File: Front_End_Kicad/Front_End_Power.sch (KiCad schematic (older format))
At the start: 27 parts

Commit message: Added footprints and digikey links to many of the components.  Missing is the primary amplifier
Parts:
- removed C?: C, symbol Device:C
- added C?: 10uF, Capacitor_SMD:C_1206_3216Metric, symbol Device:C
- C202, C203, C205, C206, C207, C208: renamed from C?; footprint (none) -> Capacitor_SMD:C_1206_3216Metric; part_url (none) -> https://www.digikey.com/en/products/detail/taiyo-yuden/EMK3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
- C204: renamed from C?; footprint (none) -> Capacitor_SMD:C_1206_3216Metric; part_url (none) -> https://www.digikey.com/en/products/detail/w%C3%BCrth-elekt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
- U201: renamed from U?; footprint (none) -> Package_TO_SOT_SMD:SOT-23-5
- gave numbers to parts that had none: 18
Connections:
- net at U201.3 (C1-): now also C?.1
- net at U201.5 (C1+): now also C?.2
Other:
- note added: "DC Offset Indication\n\n"
- moved on the sheet: C203, C204, D202, D204, D205, R201, R202, R204, TP201

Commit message: Started work on PCB.  Sections seperated and partially connected.  Planning 4 layer
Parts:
- TP201, TP202, TP203: footprint TestPoint:TestPoint_THTPad_3.0x3.0mm_Drill1.5mm -> TestPoint:TestPoint_THTPad_1.5x1.5mm_Drill0.7mm
- gave numbers to parts that had none: 1
- renumbered R203 to R202, R202 to R203
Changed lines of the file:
@@
 F 0 "TP201" H 3642 1576 50  0000 R CNN
 F 1 "v_-5v" H 3642 1667 50  0000 R CNN
-F 2 "TestPoint:TestPoint_THTPad_3.0x3.0mm_Drill1.5mm" H 3900 1550 50  0001 C CNN
+F 2 "TestPoint:TestPoint_THTPad_1.5x1.5mm_Drill0.7mm" H 3900 1550 50  0001 C CNN
 F 3 "~" H 3900 1550 50  0001 C CNN
 	1    3700 1550
@@
 F 0 "TP203" H 5192 2026 50  0000 R CNN
 F 1 "v_offset" H 5192 2117 50  0000 R CNN
-F 2 "TestPoint:TestPoint_THTPad_3.0x3.0mm_Drill1.5mm" H 5450 2000 50  0001 C CNN
+F 2 "TestPoint:TestPoint_THTPad_1.5x1.5mm_Drill0.7mm" H 5450 2000 50  0001 C CNN
 F 3 "~" H 5450 2000 50  0001 C CNN
 	1    5250 2000
@@
 P 5050 2450
 AR Path="/5FFB77CD" Ref="#PWR?"  Part="1"
-AR Path="/5FF76298/5FFB77CD" Ref="#PWR0208"  Part="1"
-F 0 "#PWR0208" H 5050 2200 50  0001 C CNN
+AR Path="/5FF76298/5FFB77CD" Ref="#PWR0214"  Part="1"
+F 0 "#PWR0214" H 5050 2200 50  0001 C CNN
 F 1 "GND" H 5055 2277 50  0000 C CNN
 F 2 "" H 5050 2450 50  0001 C CNN
@@
 	5050 2150 5050 2000
 $Comp
-L power:GND #PWR0204
+L power:GND #PWR0205
 U 1 1 5FFFF575
 P 2300 3950
-F 0 "#PWR0204" H 2300 3700 50  0001 C CNN
+F 0 "#PWR0205" H 2300 3700 50  0001 C CNN
 F 1 "GND" H 2305 3777 50  0000 C CNN
 F 2 "" H 2300 3950 50  0001 C CNN
@@
 $EndComp
 $Comp
-L power:GND #PWR0206
+L power:GND #PWR0210
 U 1 1 60002F8D
 P 4000 3950
-F 0 "#PWR0206" H 4000 3700 50  0001 C CNN
+F 0 "#PWR0210" H 4000 3700 50  0001 C CNN
 F 1 "GND" H 4005 3777 50  0000 C CNN
 F 2 "" H 4000 3950 50  0001 C CNN
@@
 P 4600 3750
 AR Path="/6004625D" Ref="R?"  Part="1"
-AR Path="/5FF76298/6004625D" Ref="R203"  Part="1"
-F 0 "R203" V 4393 3750 50  0000 C CNN
+AR Path="/5FF76298/6004625D" Ref="R202"  Part="1"
+F 0 "R202" V 4393 3750 50  0000 C CNN
 F 1 "560" V 4484 3750 50  0000 C CNN
 F 2 "Resistor_SMD:R_1206_3216Metric" V 4530 3750 50  0001 C CNN
@@
 P 3450 2150
 AR Path="/6005BA7C" Ref="#PWR?"  Part="1"
-AR Path="/5FF76298/6005BA7C" Ref="#PWR0205"  Part="1"
-F 0 "#PWR0205" H 3450 1900 50  0001 C CNN
+AR Path="/5FF76298/6005BA7C" Ref="#PWR0208"  Part="1"
+F 0 "#PWR0208" H 3450 1900 50  0001 C CNN
 F 1 "GND" H 3455 1977 50  0000 C CNN
 F 2 "" H 3450 2150 50  0001 C CNN
@@
 F 0 "TP202" H 4892 3676 50  0000 R CNN
 F 1 "v_+5v" H 4892 3767 50  0000 R CNN
-F 2 "TestPoint:TestPoint_THTPad_3.0x3.0mm_Drill1.5mm" H 5150 3650 50  0001 C CNN
+F 2 "TestPoint:TestPoint_THTPad_1.5x1.5mm_Drill0.7mm" H 5150 3650 50  0001 C CNN
 F 3 "~" H 5150 3650 50  0001 C CNN
 	1    4950 3650
@@
 P 4650 1000
 AR Path="/60066B90" Ref="R?"  Part="1"
-AR Path="/5FF76298/60066B90" Ref="R202"  Part="1"
-F 0 "R202" V 4443 1000 50  0000 C CNN
+AR Path="/5FF76298/60066B90" Ref="R203"  Part="1"
+F 0 "R203" V 4443 1000 50  0000 C CNN
 F 1 "1000" V 4534 1000 50  0000 C CNN
 F 2 "Resistor_SMD:R_1206_3216Metric" V 4580 1000 50  0001 C CNN
@@
 P 4450 1000
 AR Path="/6007290B" Ref="#PWR?"  Part="1"
-AR Path="/5FF76298/6007290B" Ref="#PWR0207"  Part="1"
-F 0 "#PWR0207" H 4450 750 50  0001 C CNN
+AR Path="/5FF76298/6007290B" Ref="#PWR0212"  Part="1"
+F 0 "#PWR0212" H 4450 750 50  0001 C CNN
 F 1 "GND" H 4455 827 50  0000 C CNN
 F 2 "" H 4450 1000 50  0001 C CNN
@@
 P 5950 1000
 AR Path="/60073F71" Ref="#PWR?"  Part="1"
-AR Path="/5FF76298/60073F71" Ref="#PWR0209"  Part="1"
-F 0 "#PWR0209" H 5950 750 50  0001 C CNN
+AR Path="/5FF76298/60073F71" Ref="#PWR0215"  Part="1"
+F 0 "#PWR0215" H 5950 750 50  0001 C CNN
 F 1 "GND" H 5955 827 50  0000 C CNN
 F 2 "" H 5950 1000 50  0001 C CNN
@@
 P 2650 1900
 AR Path="/5FBD321D" Ref="#PWR?"  Part="1"
-AR Path="/5FF76298/5FBD321D" Ref="#PWR?"  Part="1"
-F 0 "#PWR?" H 2650 1650 50  0001 C CNN
+AR Path="/5FF76298/5FBD321D" Ref="#PWR0206"  Part="1"
+F 0 "#PWR0206" H 2650 1650 50  0001 C CNN
 F 1 "GND" H 2655 1727 50  0000 C CNN
 F 2 "" H 2650 1900 50  0001 C CNN
@@
 P 900 1350
 AR Path="/5FBD4F62" Ref="C?"  Part="1"
-AR Path="/5FF76298/5FBD4F62" Ref="C?"  Part="1"
-F 0 "C?" V 1152 1350 50  0000 C CNN
+AR Path="/5FF76298/5FBD4F62" Ref="C201"  Part="1"
+F 0 "C201" V 1152 1350 50  0000 C CNN
 F 1 "10uF" V 1061 1350 50  0000 C CNN
 F 2 "Capacitor_SMD:C_1206_3216Metric" H 938 1200 50  0001 C CNN
@@
 	2300 3900 2300 3950
 $Comp
-L power:GND #PWR?
+L power:GND #PWR0204
 U 1 1 5FBDD8CE
 P 2050 3950
-F 0 "#PWR?" H 2050 3700 50  0001 C CNN
+F 0 "#PWR0204" H 2050 3700 50  0001 C CNN
 F 1 "GND" H 2055 3777 50  0000 C CNN
 F 2 "" H 2050 3950 50  0001 C CNN
@@
 $EndComp
 $Comp
-L power:GND #PWR?
+L power:GND #PWR0203
 U 1 1 5FBE062F
 P 1350 3950
-F 0 "#PWR?" H 1350 3700 50  0001 C CNN
+F 0 "#PWR0203" H 1350 3700 50  0001 C CNN
 F 1 "GND" H 1355 3777 50  0000 C CNN
 F 2 "" H 1350 3950 50  0001 C CNN
@@
 $EndComp
 $Comp
-L power:GND #PWR?
+L power:GND #PWR0207
 U 1 1 5FBE4917
 P 3050 3950
-F 0 "#PWR?" H 3050 3700 50  0001 C CNN
+F 0 "#PWR0207" H 3050 3700 50  0001 C CNN
 F 1 "GND" H 3055 3777 50  0000 C CNN
 F 2 "" H 3050 3950 50  0001 C CNN
@@
 $EndComp
 $Comp
-L power:GND #PWR?
+L power:GND #PWR0209
 U 1 1 5FBE7790
 P 3500 3950
-F 0 "#PWR?" H 3500 3700 50  0001 C CNN
+F 0 "#PWR0209" H 3500 3700 50  0001 C CNN
 F 1 "GND" H 3505 3777 50  0000 C CNN
 F 2 "" H 3500 3950 50  0001 C CNN
@@
 	3500 3950 3500 3850
 $Comp
-L power:GND #PWR?
+L power:GND #PWR0211
 U 1 1 5FBECE27
 P 4200 3950
-F 0 "#PWR?" H 4200 3700 50  0001 C CNN
+F 0 "#PWR0211" H 4200 3700 50  0001 C CNN
 F 1 "GND" H 4205 3777 50  0000 C CNN
 F 2 "" H 4200 3950 50  0001 C CNN
@@
 $EndComp
 $Comp
-L power:GND #PWR?
+L power:GND #PWR0213
 U 1 1 5FBEF606
 P 4600 4300
-F 0 "#PWR?" H 4600 4050 50  0001 C CNN
+F 0 "#PWR0213" H 4600 4050 50  0001 C CNN
 F 1 "GND" H 4605 4127 50  0000 C CNN
 F 2 "" H 4600 4300 50  0001 C CNN

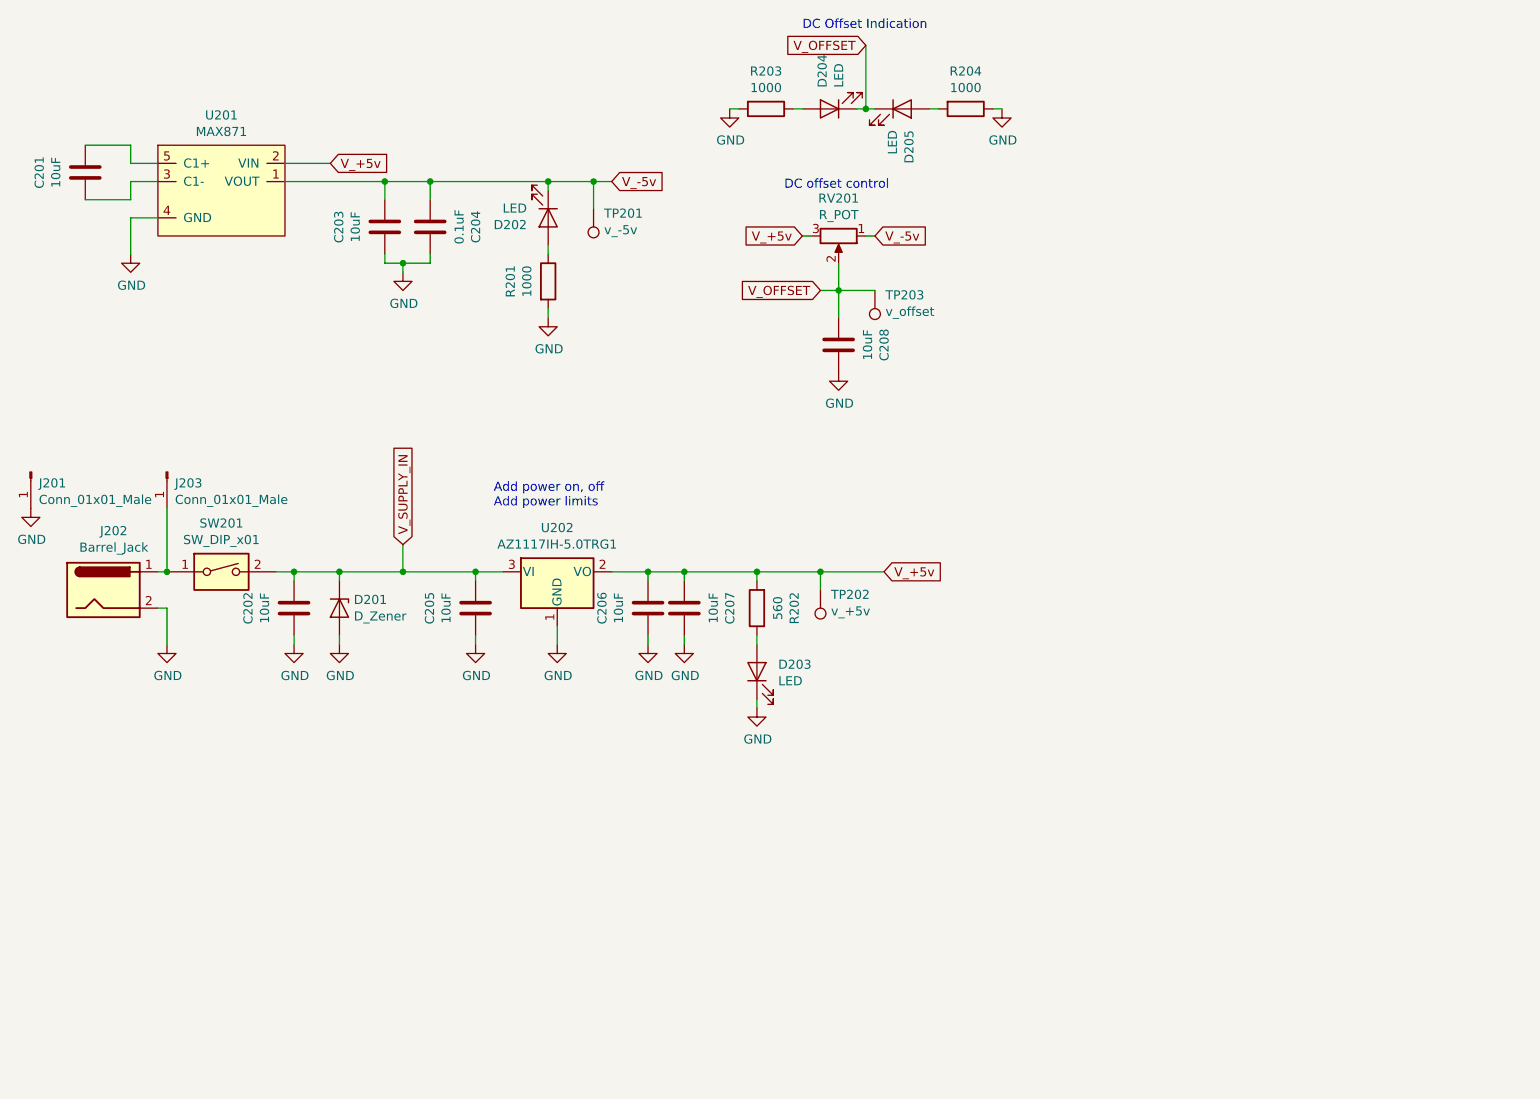
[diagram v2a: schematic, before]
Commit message: PCB nearly complete.  Added schematics and layers
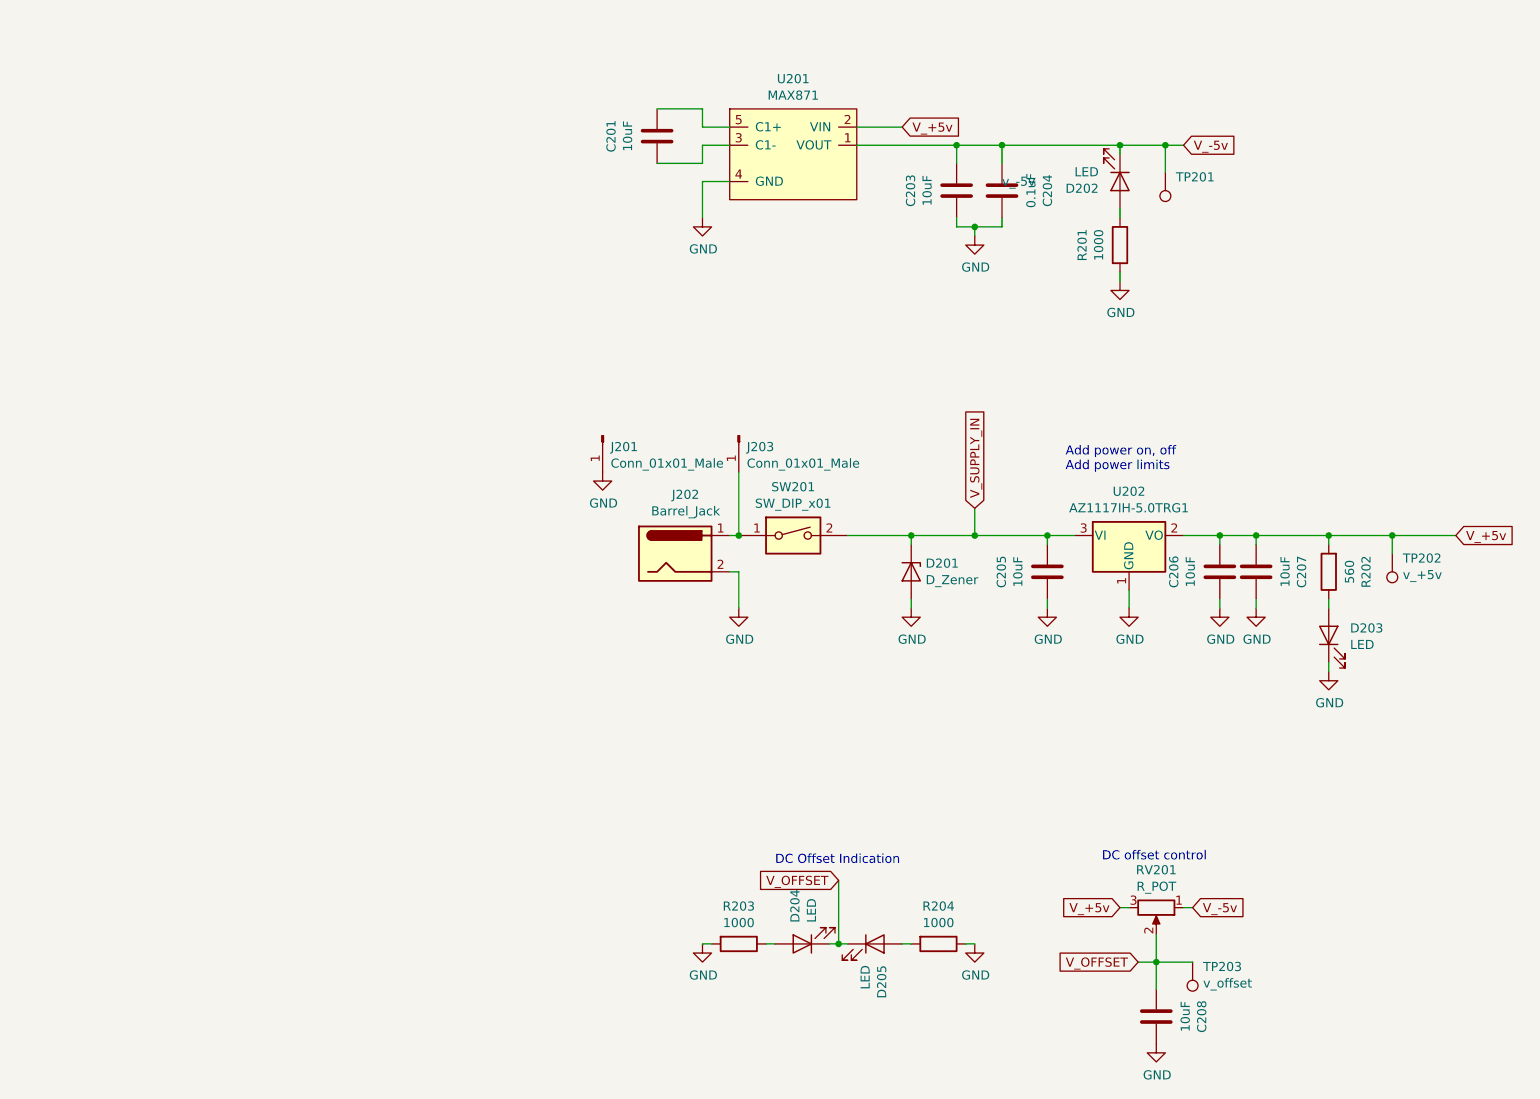
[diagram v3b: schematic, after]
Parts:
- removed C202: 10uF, Capacitor_SMD:C_1206_3216Metric, symbol Device:C
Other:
- moved on the sheet: C201, C203, C204, C205, C206, C207, C208, D201, D202, D203, D204, D205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

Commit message: Added names to parts to show better
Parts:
- C201, C203, C204, C205, C206, C207, C208: part_name (none) -> Bypass Cap
- J201, J203: part_name (none) -> Male Header
- R201, R202, R203, R204: part_name (none) -> Resistor
- RV201: part_name (none) -> Potentiometer
- SW201: part_name (none) -> Power Switch
- U201: part_name max871 -> Max871
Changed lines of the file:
@@
 F 3 "" H 4600 850 50  0001 C CNN
 F 4 "Negative voltage regulator" H 4600 850 50  0001 C CNN "part_description"
-F 5 "max871" H 4600 850 50  0001 C CNN "part_name"
+F 5 "Max871" H 4600 850 50  0001 C CNN "part_name"
 F 6 "https://www.digikey.com/en/products/detail/maxim-integrated/MAX871EUK-T/1519057" H 4600 850 50  0001 C CNN "part_url"
 	1    4600 850
@@
 F 3 "~" H 5700 1450 50  0001 C CNN
 F 4 "https://www.digikey.com/en/products/detail/taiyo-yuden/EMK316BJ106KL-T/930691" H 5700 1450 50  0001 C CNN "part_url"
+F 5 "Bypass Cap" H 5700 1450 50  0001 C CNN "part_name"
 	1    5700 1450
 	-1   0    0    1
@@
 F 3 "~" H 5950 1450 50  0001 C CNN
 F 4 "https://www.digikey.com/en/products/detail/w%C3%BCrth-elektronik/885012208030/5453952" H 5950 1450 50  0001 C CNN "part_url"
+F 5 "Bypass Cap" H 5950 1450 50  0001 C CNN "part_name"
 	1    5950 1450
 	1    0    0    -1
@@
 F 4 "DC voltage offset" H 6800 5400 50  0001 C CNN "part_description"
 F 5 "https://www.digikey.com/en/products/detail/tt-electronics-bi/P120PK-Y25BR10K/5957454" H 6800 5400 50  0001 C CNN "part_url"
+F 6 "Potentiometer" H 6800 5400 50  0001 C CNN "part_name"
 	1    6800 5400
 	0    1    1    0
@@
 F 3 "~" H 6800 6000 50  0001 C CNN
 F 4 "https://www.digikey.com/en/products/detail/taiyo-yuden/EMK316BJ106KL-T/930691" H 6800 6000 50  0001 C CNN "part_url"
+F 5 "Bypass Cap" H 6800 6000 50  0001 C CNN "part_name"
 	1    6800 6000
 	1    0    0    -1
@@
 F 3 "~" H 6200 3550 50  0001 C CNN
 F 4 "https://www.digikey.com/en/products/detail/taiyo-yuden/EMK316BJ106KL-T/930691" H 6200 3550 50  0001 C CNN "part_url"
+F 5 "Bypass Cap" H 6200 3550 50  0001 C CNN "part_name"
 	1    6200 3550
 	-1   0    0    1
@@
 F 3 "~" H 7150 3550 50  0001 C CNN
 F 4 "https://www.digikey.com/en/products/detail/taiyo-yuden/EMK316BJ106KL-T/930691" H 7150 3550 50  0001 C CNN "part_url"
+F 5 "Bypass Cap" H 7150 3550 50  0001 C CNN "part_name"
 	1    7150 3550
 	-1   0    0    1
@@
 F 3 "~" H 4800 3350 50  0001 C CNN
 F 4 "Power toggle switch" H 4800 3350 50  0001 C CNN "part_description"
+F 5 "Power Switch" H 4800 3350 50  0001 C CNN "part_name"
 	1    4800 3350
 	1    0    0    -1
@@
 F 3 "~" H 7750 3550 50  0001 C CNN
 F 4 "https://www.digikey.com/en/products/detail/te-connectivity-passive-product/CRGCQ1206F560R/8576409" V 7750 3550 50  0001 C CNN "part_url"
+F 5 "Resistor" H 7750 3550 50  0001 C CNN "part_name"
 	1    7750 3550
 	-1   0    0    1
@@
 F 3 "~" H 4500 5600 50  0001 C CNN
 F 4 "https://www.digikey.com/en/products/detail/stackpole-electronics-inc/RNCP1206FTD1K00/2240337" V 4500 5600 50  0001 C CNN "part_url"
+F 5 "Resistor" H 4500 5600 50  0001 C CNN "part_name"
 	1    4500 5600
 	0    1    1    0
@@
 F 3 "~" H 5600 5600 50  0001 C CNN
 F 4 "https://www.digikey.com/en/products/detail/stackpole-electronics-inc/RNCP1206FTD1K00/2240337" V 5600 5600 50  0001 C CNN "part_url"
+F 5 "Resistor" H 5600 5600 50  0001 C CNN "part_name"
 	1    5600 5600
 	0    1    1    0
@@
 F 3 "~" H 6600 1750 50  0001 C CNN
 F 4 "https://www.digikey.com/en/products/detail/stackpole-electronics-inc/RNCP1206FTD1K00/2240337" V 6600 1750 50  0001 C CNN "part_url"
+F 5 "Resistor" H 6600 1750 50  0001 C CNN "part_name"
 	1    6600 1750
 	1    0    0    -1
@@
 F 2 "Connector_PinHeader_2.00mm:PinHeader_1x01_P2.00mm_Vertical" H 4500 2800 50  0001 C CNN
 F 3 "~" H 4500 2800 50  0001 C CNN
+F 4 "Male Header" H 4500 2800 50  0001 C CNN "part_name"
 	1    4500 2800
 	0    1    1    0
@@
 F 2 "Connector_PinHeader_2.00mm:PinHeader_1x01_P2.00mm_Vertical" H 3750 2800 50  0001 C CNN
 F 3 "~" H 3750 2800 50  0001 C CNN
+F 4 "Male Header" H 3750 2800 50  0001 C CNN "part_name"
 	1    3750 2800
 	0    1    1    0
@@
 F 3 "~" H 4050 1150 50  0001 C CNN
 F 4 "https://www.digikey.com/en/products/detail/taiyo-yuden/EMK316BJ106KL-T/930691" H 4050 1150 50  0001 C CNN "part_url"
+F 5 "Bypass Cap" H 4050 1150 50  0001 C CNN "part_name"
 	1    4050 1150
 	-1   0    0    1
@@
 F 3 "~" H 7350 3550 50  0001 C CNN
 F 4 "https://www.digikey.com/en/products/detail/taiyo-yuden/EMK316BJ106KL-T/930691" H 7350 3550 50  0001 C CNN "part_url"
+F 5 "Bypass Cap" H 7350 3550 50  0001 C CNN "part_name"
 	1    7350 3550
 	1    0    0    -1

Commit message: Updated schematic
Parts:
- D204, D205: part_name LED Green -> LED Red; part_url https://www.digikey.com/en/products/detail/w%C3%BCrth-elektronik/150120GS75000/4489936 -> https://www.digikey.com/en/products/detail/w%C3%BCrth-elektronik/156120RS75000/4490056
- J201: value Conn_01x01_Male -> Gnd
- J203: value Conn_01x01_Male -> External_Power
- SW201: value SW_DIP_x01 -> power_switch
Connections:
- net GND: now also C205.2; no longer C205.1
- net V_SUPPLY_IN: now also C205.1; no longer C205.2
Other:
- note added: "+11v Zener on"
- note added: "+5V Regulator"
- note added: "+6V to +10V"
- note added: "-5V voltage generator"
- note added: "Adjustable DC Offset"
- note added: "External Power\n"
- note removed: "Add power on, off\nAdd power limits"
- moved on the sheet: C201, C203, C204, C205, C206, C207, C208, D201, D202, D203, D204, D205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
